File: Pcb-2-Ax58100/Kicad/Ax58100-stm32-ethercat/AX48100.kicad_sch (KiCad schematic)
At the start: 33 parts, among them U1 AX58100, U2 24LC32A, Y1 NXK25.000AE12F-KAB6-12

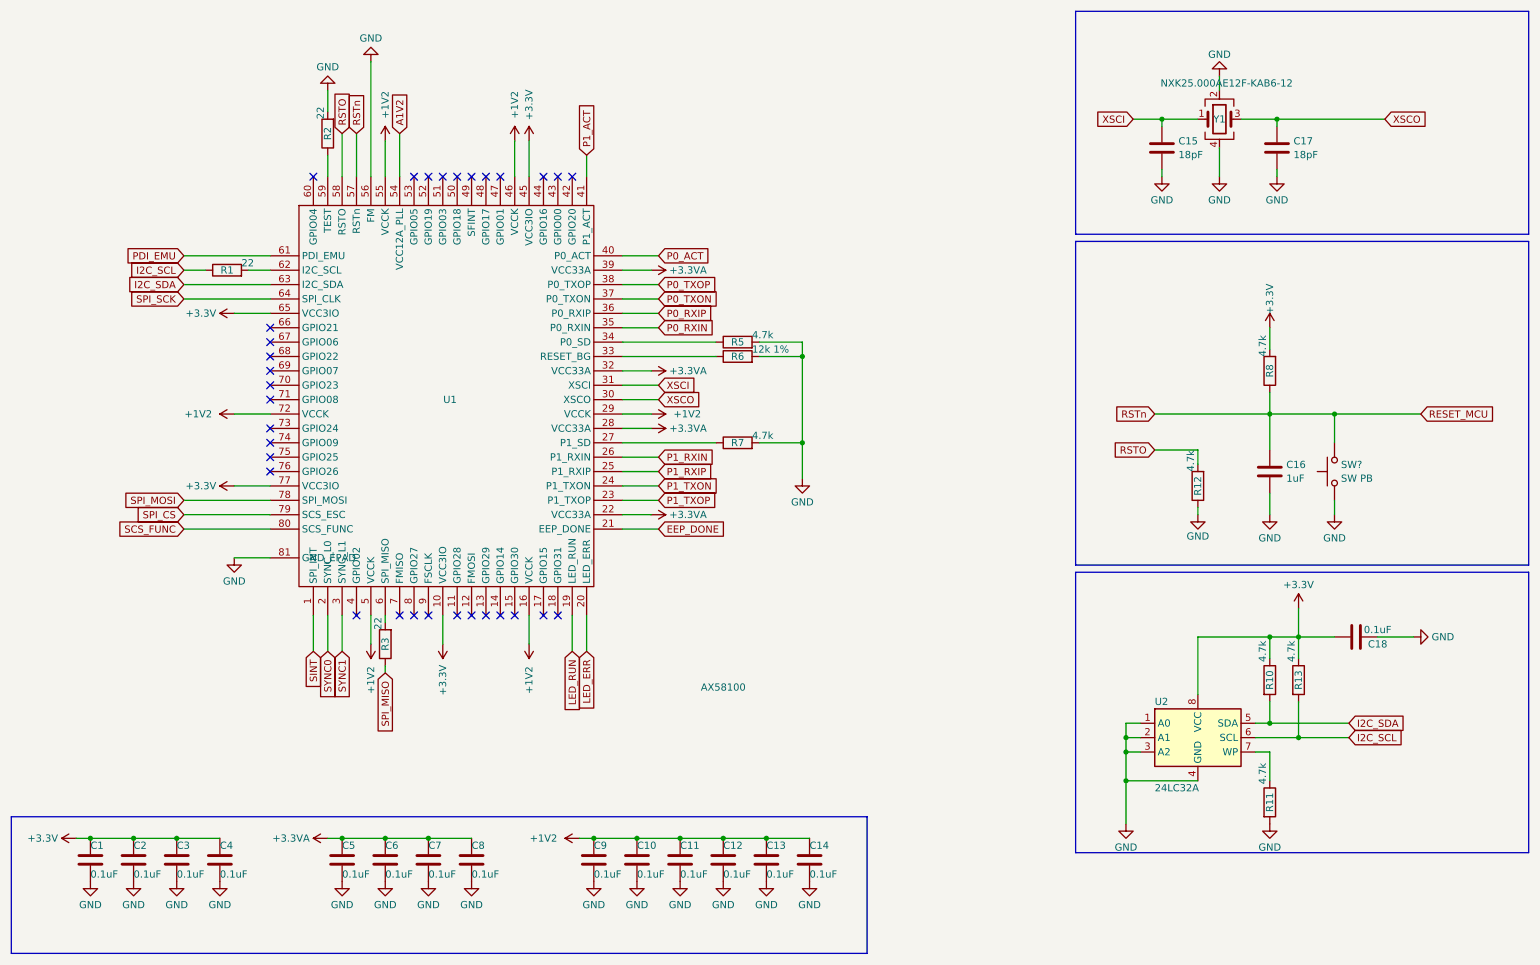
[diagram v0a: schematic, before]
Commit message: Geographic annotation on pcb 2
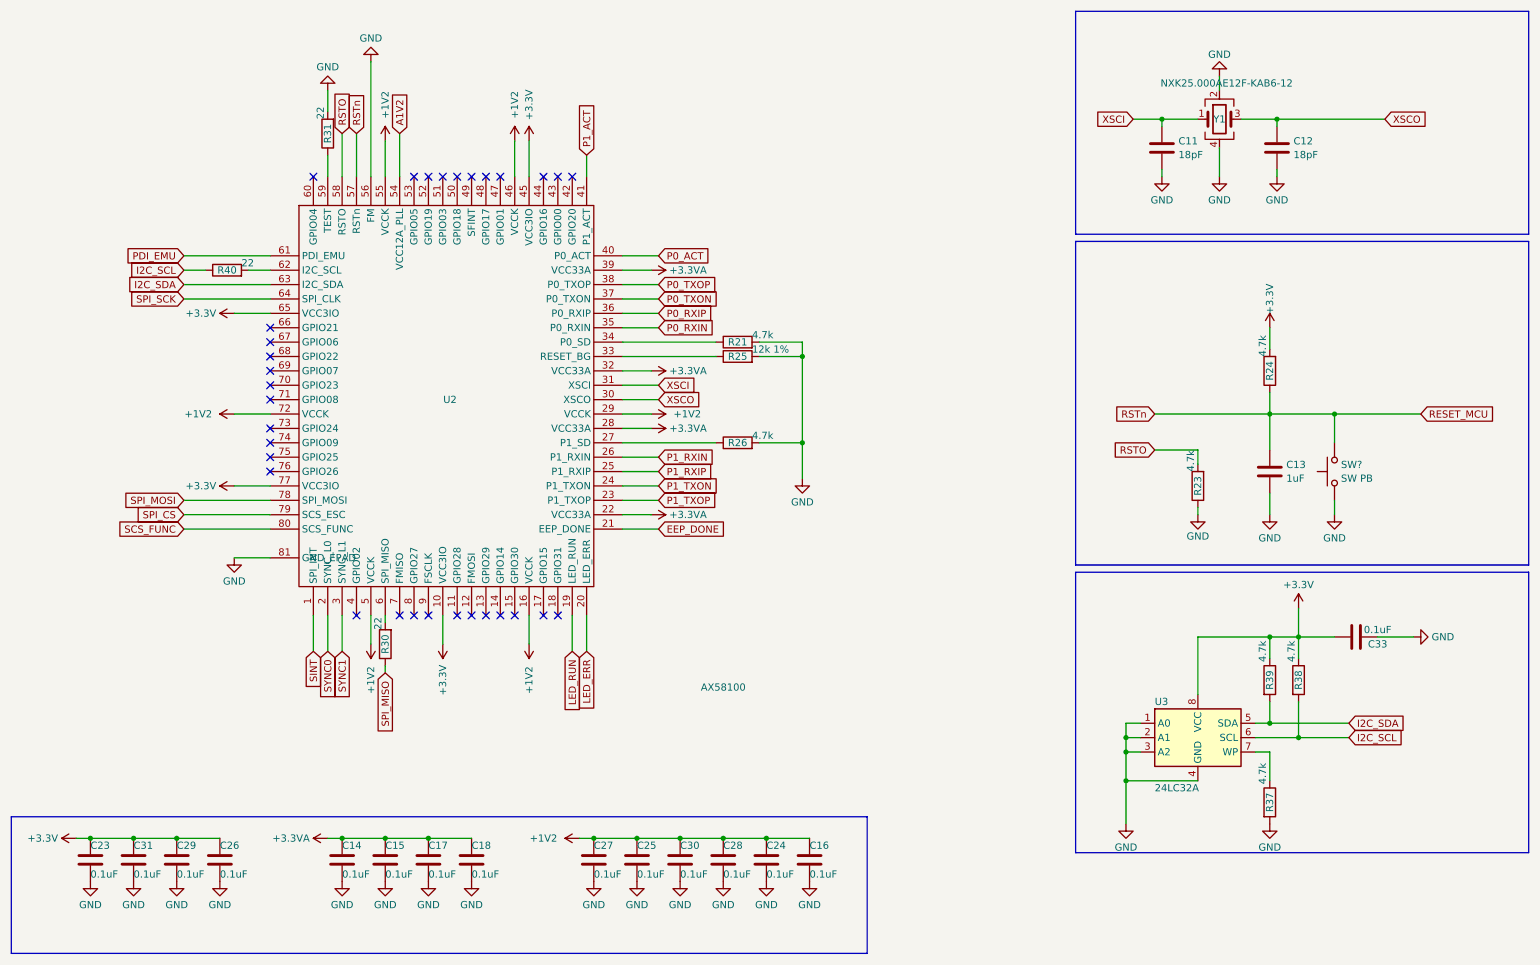
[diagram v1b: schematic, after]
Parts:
- renumbered C15 to C11, C17 to C12, C16 to C13, C5 to C14, C6 to C15, C14 to C16, C7 to C17, C8 to C18, C1 to C23, C13 to C24, C10 to C25, C4 to C26, C9 to C27, C12 to C28, C3 to C29, C11 to C30, C2 to C31, C18 to C33, R5 to R21, R12 to R23, R8 to R24, R6 to R25, R7 to R26, R3 to R30, R2 to R31, R11 to R37, R13 to R38, R10 to R39, R1 to R40, U1 to U2, U2 to U3
